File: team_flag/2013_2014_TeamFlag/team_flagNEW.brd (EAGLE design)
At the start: 40.3 x 40.6 mm, 9 parts, among them Q1 MOSFET-NCHANNELSMD, Q2 MOSFET-NCHANNELSMD

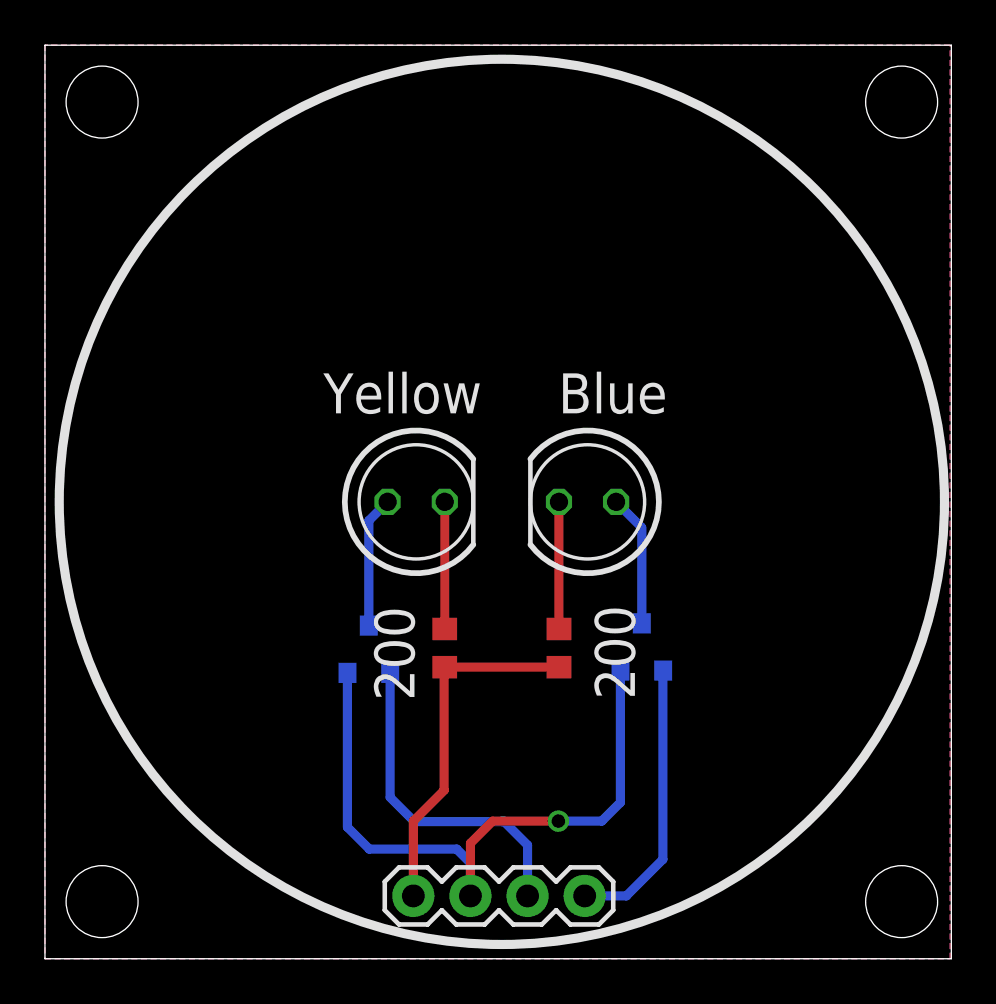
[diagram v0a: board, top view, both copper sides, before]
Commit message: Team Flag - Rev A
-Rewired MOSFETs correctly
-Repositioned bottom silkscreen text and updated information
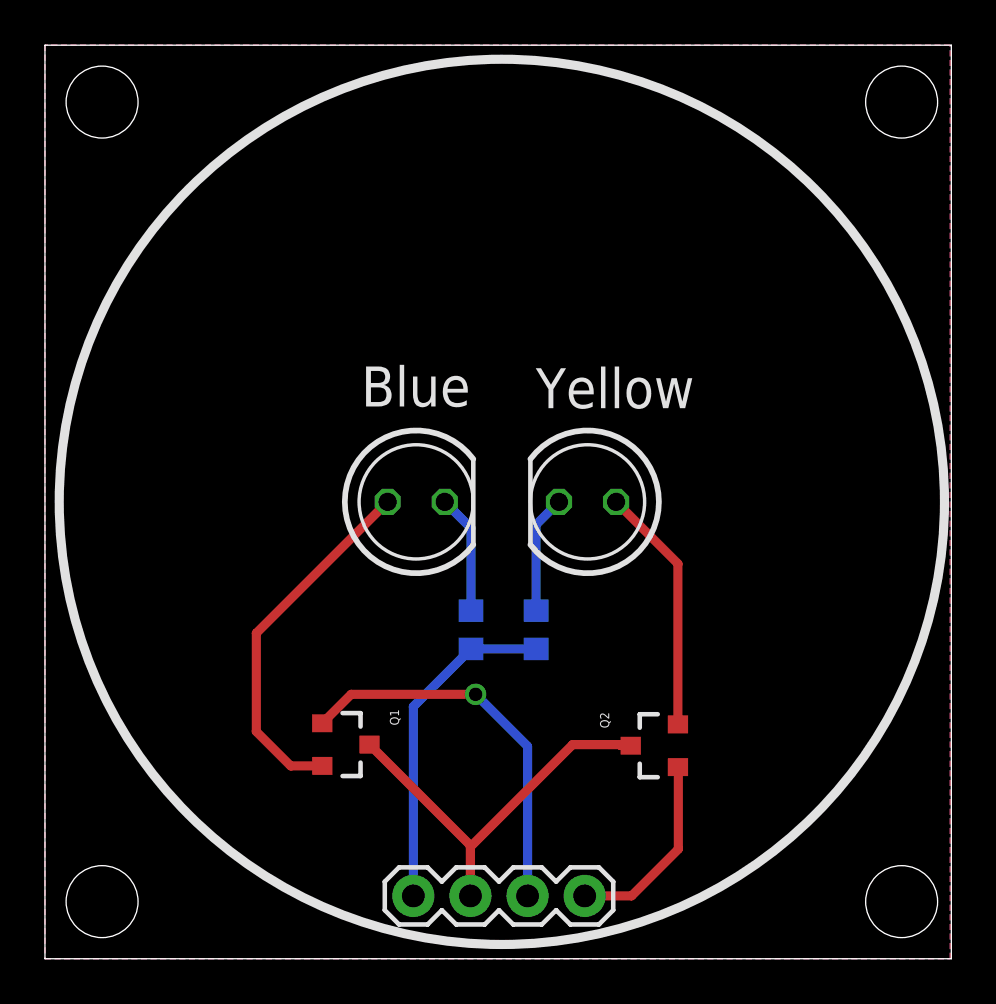
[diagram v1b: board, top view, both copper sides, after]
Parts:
- R1, R2: value (none) -> 330
- moved U$2 21.1 mm to (20.1, 31.2)
- moved Q2 4.39 mm to (27.2, 9.47), flipped to the top, turned to 90 degrees
- moved Q1 4.32 mm to (13.3, 9.53), flipped to the top, turned to 270 degrees
- moved R1 1.42 mm to (18.9, 14.6), flipped to the bottom
- moved R2 1.30 mm to (21.8, 14.6), flipped to the bottom
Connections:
- net 5V: now also Q1.3, Q2.3; no longer Q1.2, Q2.2
- net BDRAIN: now also LED1.K, R1.2; no longer LED2.K, R2.2
- net BLUE: now also JP1.3, Q1.1; no longer JP1.4, Q2.1
- net BSIGNAL: now also LED1.A, Q1.2; no longer LED2.A, Q2.3
- net YDRAIN: now also LED2.K, R2.2; no longer LED1.K, R1.2
- net YELLOW: now also JP1.4, Q2.1; no longer JP1.3, Q1.1
- net YSIGNAL: now also LED2.A, Q2.2; no longer LED1.A, Q1.3
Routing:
- net BSIGNAL: track 5.88 -> 16.2 mm
- net 5V: track 30.1 -> 20.3 mm, vias 1 -> 0
- net YELLOW: track 14.8 -> 8.68 mm
- net YSIGNAL: track 5.85 -> 11.0 mm
- net BLUE: track 12.6 -> 17.3 mm, vias 0 -> 1
- net GND: track 15.8 -> 14.9 mm
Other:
- board text added: "Version 3.0, Rev A"
- board text removed: "200"
